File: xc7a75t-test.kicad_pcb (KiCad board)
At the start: 6 copper layers, 150 parts, among them IC1 IS25LP256D-JLLE, J1 jtag_header_01x06, Q1 FDS9926A, SW1 SW_Push, U1 XC7A75T-FTG256, U2 ADP5052ACPZ-R7

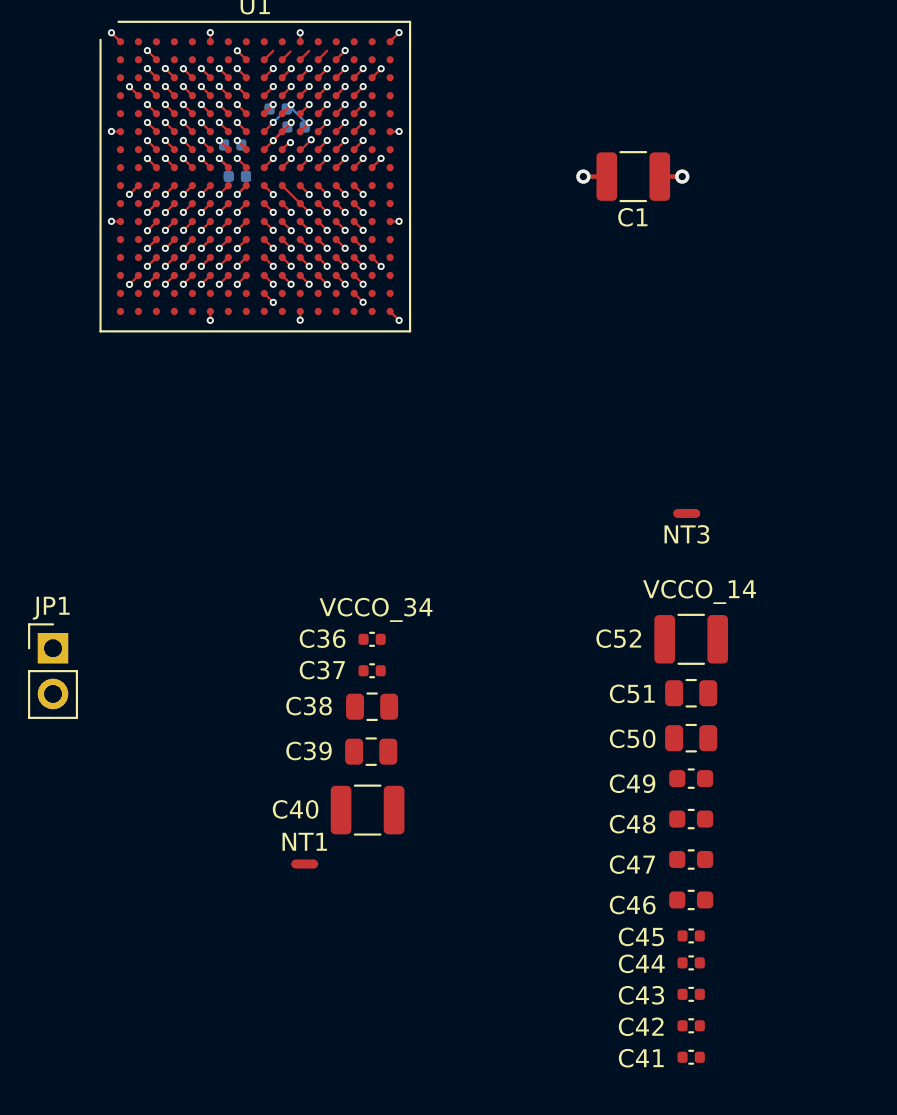
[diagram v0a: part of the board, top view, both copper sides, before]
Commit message: Add power plane setup
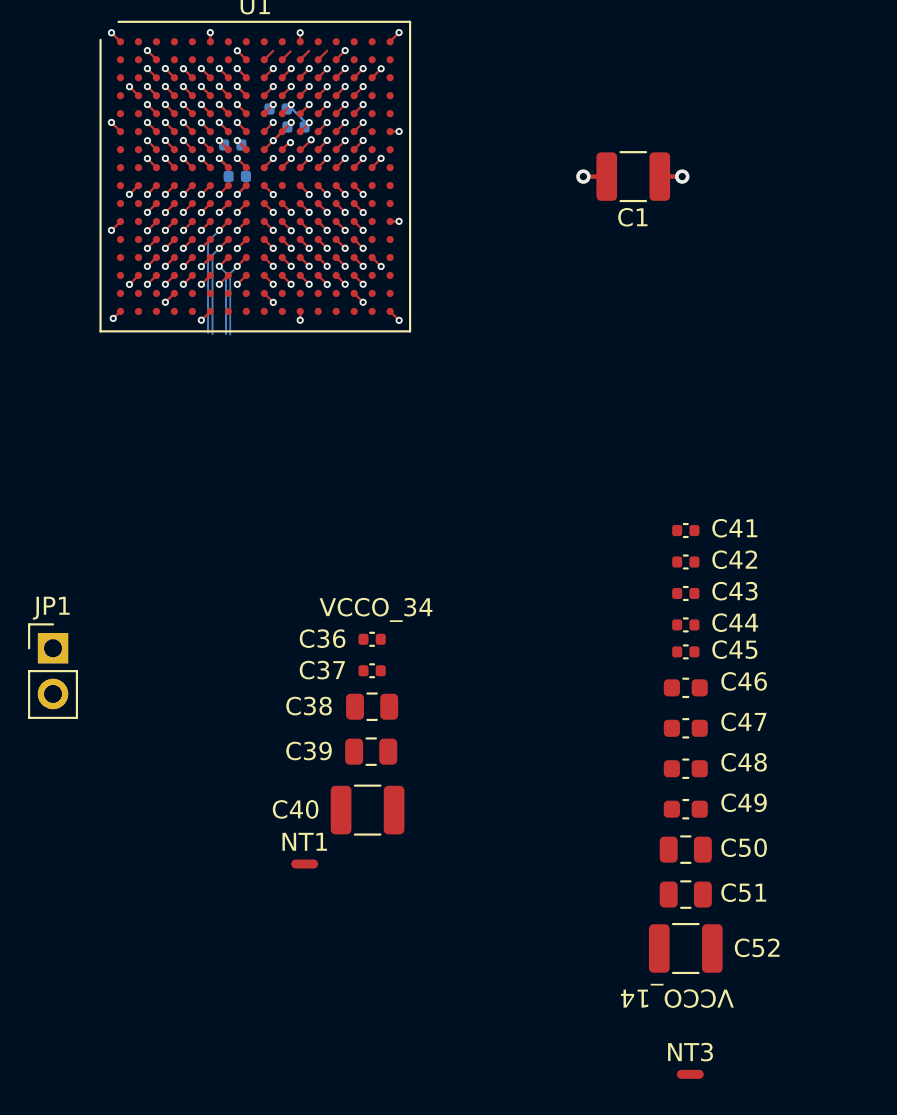
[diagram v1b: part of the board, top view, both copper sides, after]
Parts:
- moved NT3 31.2 mm to (158.5, 149.3), turned to 0 degrees
- moved C41 29.3 mm to (158.2, 119.0), turned to 180 degrees
- moved C42 25.8 mm to (158.2, 120.8), turned to 180 degrees
- moved C43 22.3 mm to (158.2, 122.5), turned to 180 degrees
- moved C44 18.8 mm to (158.2, 124.3), turned to 180 degrees
- moved C52 17.2 mm to (158.2, 142.3), turned to 180 degrees
- moved C45 15.8 mm to (158.2, 125.8), turned to 180 degrees
- moved C46 11.8 mm to (158.2, 127.8), turned to 180 degrees
- moved C51 11.2 mm to (158.2, 139.3), turned to 180 degrees
- moved C47 7.31 mm to (158.2, 130.0), turned to 180 degrees
- moved C50 6.21 mm to (158.2, 136.8), turned to 180 degrees
- moved C48 2.82 mm to (158.2, 132.3), turned to 180 degrees
- moved C49 1.73 mm to (158.2, 134.5), turned to 180 degrees
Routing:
- net VCCBRAM: track 1.30 -> 13.1 mm, vias 1 -> 3
- net VCCINT: track 4.26 -> 11.3 mm, vias 6 -> 7
- net +1V8: track 0.72 -> 7.56 mm
- net VCCO_0: track 0.71 -> 7.50 mm
- net /sheet60847A1B/JTAG_TCK_O: track 10.0 -> 16.0 mm
- net SNS0V95-: track 5.49 -> 0.00 mm, vias 3 -> 0
- net /sheet60847A1B/JTAG_TMS_O: track 0.71 -> 5.64 mm
- net /sheet60847A1B/JTAG_TDO_O: track 0.71 -> 4.67 mm
- net /sheet60847A1B/JTAG_TDI_O: track 0.71 -> 4.64 mm
- net VCCAUX: track 3.55 -> 2.13 mm
- net VCCO_34: track 0.71 -> 1.98 mm, vias 1 -> 3
- added copper zone on 4pwr.Cu, net VCCAUX
- added copper zone on 4pwr.Cu, net VCCINT
- added copper zone on 4pwr.Cu, net VCCO_14
- added copper zone on 4pwr.Cu, net VCCO_15
- added copper zone on 4pwr.Cu, net VCCO_34
- added copper zone on 4pwr.Cu, net VCCO_35
- removed copper zone on 4pwr.Cu, net +3V3
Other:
- net class BGA_power added: clearance 0.127, trace_width 0.127, via_dia 0.4, via_drill 0.2
- net class Default: clearance 0.2 -> 0.127
- net class min_signal added: clearance 0.127, trace_width 0.09, via_dia 0.4, via_drill 0.2
- net class signal: clearance 0.2 -> 0.127; trace_width 0.127 -> 0.1; via_dia 0.6 -> 0.4; via_drill 0.3 -> 0.2
- rule trace_clearance: 0.2 -> 0.127
- rule trace_min: 0.127 -> 0.09

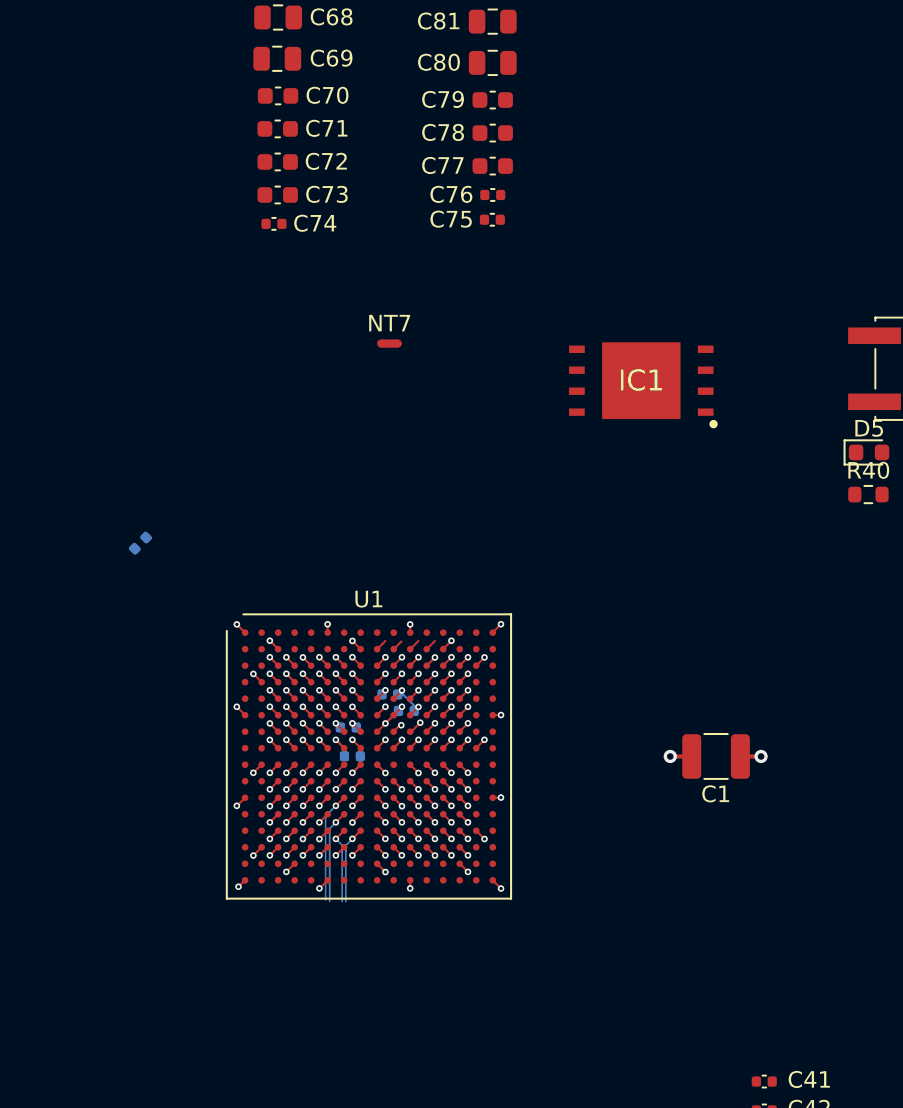
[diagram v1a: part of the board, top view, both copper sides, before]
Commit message: Add wire up for Q-SPI flash module.
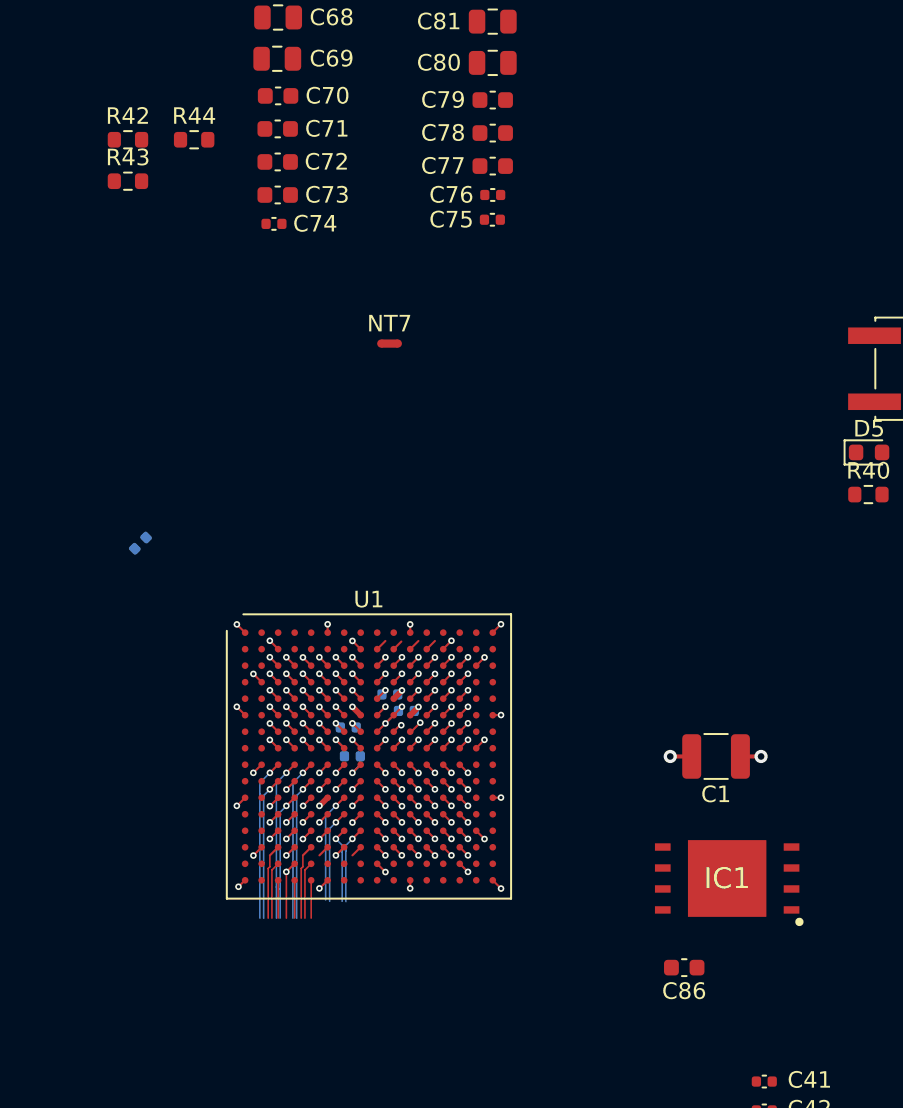
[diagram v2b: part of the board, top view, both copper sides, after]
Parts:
- added C86: 100nF, Capacitor_SMD:C_0603_1608Metric, F.Cu at (153.4, 112.1)
- added R42: 2.4k, Resistor_SMD:R_0603_1608Metric, F.Cu at (119.7, 62.0)
- added R43: 4.7k, Resistor_SMD:R_0603_1608Metric, F.Cu at (119.7, 64.5)
- added R44: 4.7k, Resistor_SMD:R_0603_1608Metric, F.Cu at (123.7, 62.0)
- moved IC1 30.6 mm to (156.0, 106.7)
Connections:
- net Net-(U1-PadJ15) renamed QSPI_FOE_B
- net Net-(U1-PadJ16) renamed QSPI_FWE_B
- net Net-(U1-PadL15) renamed QSPI_PUDC_B
- net Net-(U1-PadR13) renamed QSPI_CSI_B
- net Net-(U1-PadT12) renamed QSPI_CSO_B
- IC1 pad 1: Net-(IC1-Pad1) -> QSPI_FCS
- IC1 pad 2: Net-(IC1-Pad2) -> QSPI_DQ1
- IC1 pad 3: Net-(IC1-Pad3) -> QSPI_DQ2
- IC1 pad 5: Net-(IC1-Pad5) -> QSPI_SI
- IC1 pad 7: Net-(IC1-Pad7) -> QSPI_DQ3
- IC1 pad 9: Net-(IC1-Pad9) -> GND
- U1 pad F8: +1V8 -> GND
- U1 pad J13: Net-(U1-PadJ13) -> QSPI_SI
- U1 pad J14: Net-(U1-PadJ14) -> QSPI_DQ1
- U1 pad K15: Net-(U1-PadK15) -> QSPI_DQ2
- U1 pad K16: Net-(U1-PadK16) -> QSPI_DQ3
- U1 pad L12: Net-(U1-PadL12) -> QSPI_FCS
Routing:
- net Net-(U1-PadJ4): track 0.71 -> 9.75 mm
- net Net-(U1-PadJ5): track 0.71 -> 9.75 mm
- net Net-(U1-PadJ3): track 0.71 -> 9.75 mm
- net Net-(U1-PadK5): track 0.71 -> 8.66 mm
- net Net-(U1-PadK3): track 0.71 -> 8.66 mm
- net +1V8: track 7.56 -> 0.00 mm, vias 1 -> 0
- net GND: track 28.7 -> 36.2 mm, vias 37 -> 38
- net Net-(U1-PadL5): track 0.69 -> 7.66 mm
- net Net-(U1-PadL4): track 0.71 -> 7.66 mm
- net Net-(U1-PadL3): track 0.72 -> 7.66 mm
- net Net-(U1-PadM4): track 0.71 -> 6.71 mm
- net Net-(U1-PadM5): track 0.71 -> 6.66 mm
- net Net-(U1-PadN4): track 0.71 -> 5.77 mm
- net Net-(U1-PadN3): track 0.71 -> 5.65 mm
- net Net-(U1-PadP4): track 0.71 -> 4.66 mm
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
